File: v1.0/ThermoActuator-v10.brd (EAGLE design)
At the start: 101.6 x 53.3 mm, 18 parts

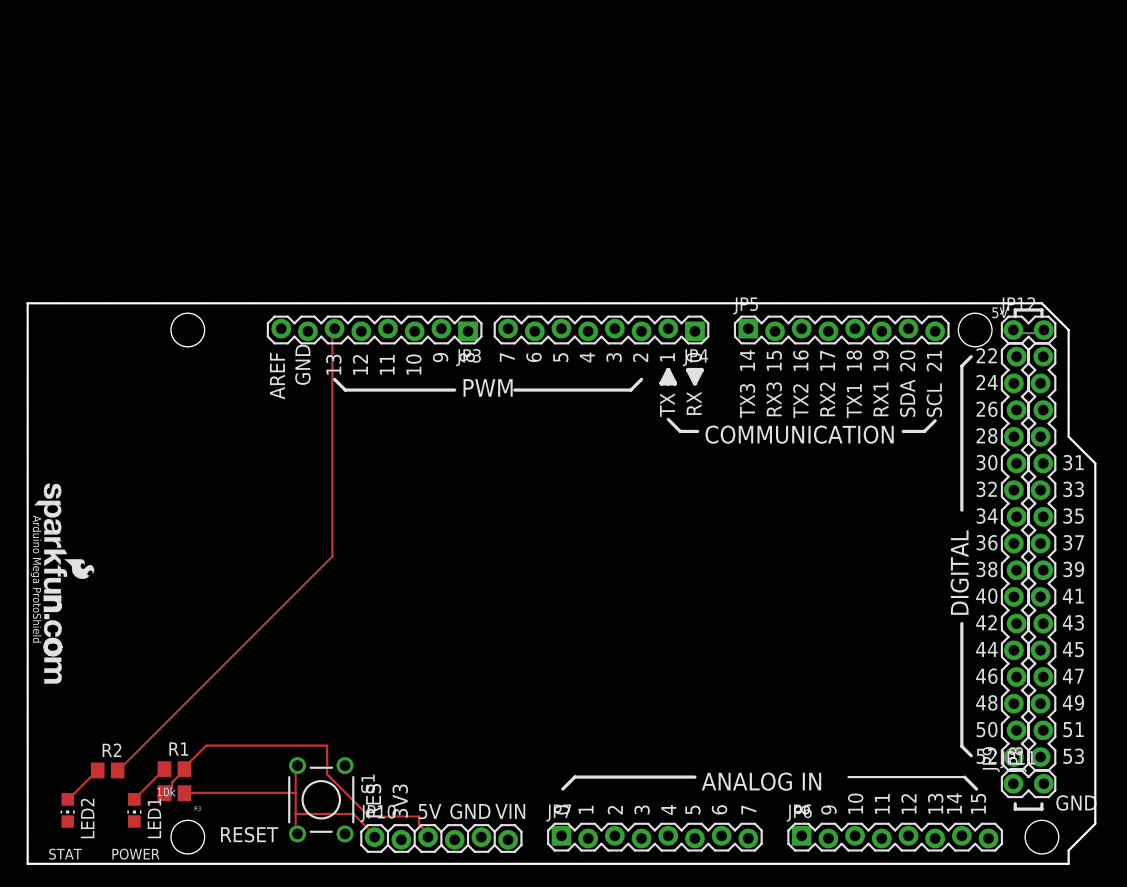
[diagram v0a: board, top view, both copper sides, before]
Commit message: one thermistor ch laid out
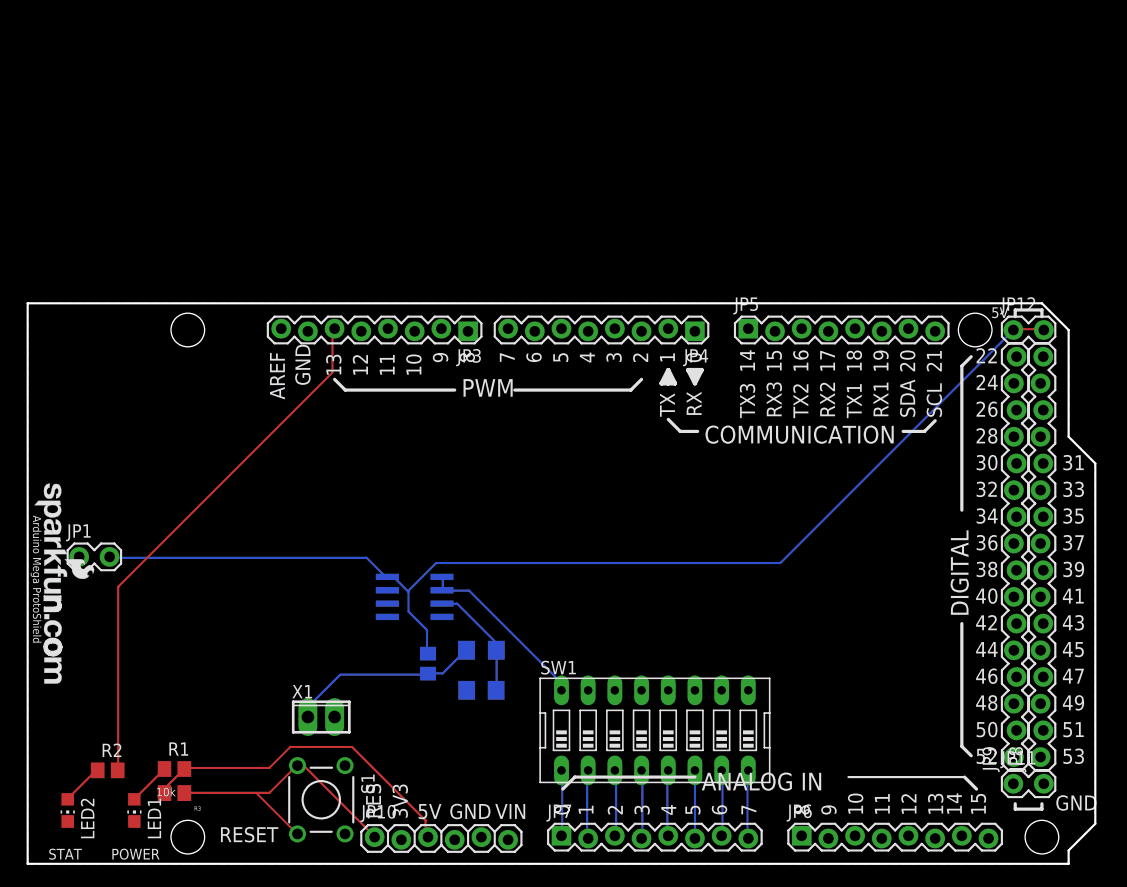
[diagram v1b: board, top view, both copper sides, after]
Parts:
- removed U$2: CREATIVE_COMMONS, SparkFun:CREATIVE_COMMONS
- added C1: 10nF, rcl:C1206
- added IC1: LM358D, linear:SO08
- added JP1: (no value), SparkFun:1X02_LOCK
- added R4: 100K, rcl:R0805
- added R5: 10K, rcl:R1206
- added SW1: (no value), special:EDG-08
- added X1: (no value), con-phoenix-254:2POL254
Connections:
- removed net 5V@1: JP12.1, JP12.2
- removed net A0: JP7.1
- removed net A1: JP7.2
- removed net A2: JP7.3
- removed net A3: JP7.4
- removed net A4: JP7.5
- removed net A5: JP7.6
- removed net A6: JP7.7
- removed net A7: JP7.8
- new net AS0: IC1.1, IC1.2, SW1.16
- new net N$1: R4.1, R5.1, X1.1
- new net N$10: JP7.8, SW1.8
- new net N$2: C1.2, IC1.3, R5.2
- new net N$3: JP7.1, SW1.1
- new net N$4: JP7.2, SW1.2
- new net N$5: JP7.3, SW1.3
- new net N$6: JP7.4, SW1.4
- new net N$7: JP7.5, SW1.5
- new net N$8: JP7.6, SW1.6
- new net N$9: JP7.7, SW1.7
- new net VDD: IC1.8, JP1.2, JP12.1, JP12.2, R4.2
- net GND: now also C1.1, IC1.4, X1.2
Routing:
- net VDD: track 0.00 -> 107.5 mm
- net N$1: track 0.00 -> 18.4 mm
- net AS0: track 0.00 -> 17.0 mm
- net N$2: track 0.00 -> 11.3 mm
- net N$4: track 0.00 -> 6.59 mm
- net N$6: track 0.00 -> 6.57 mm
- net N$10: track 0.00 -> 6.57 mm
- net N$8: track 0.00 -> 6.48 mm
- net N$5: track 0.00 -> 6.39 mm
- net N$7: track 0.00 -> 6.33 mm
- net N$9: track 0.00 -> 6.33 mm
- net N$3: track 0.00 -> 6.31 mm
- net 5V@1: track 3.12 -> 0.00 mm
- net RES: track 25.8 -> 27.6 mm
- net 5V: track 33.3 -> 31.6 mm

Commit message: two channels laid out
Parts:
- added C2: 10nF, rcl:C1206
- added R6: 100K, rcl:R0805
- added R7: 10K, rcl:R1206
- added X2: (no value), con-phoenix-254:2POL254
- moved X1 15.2 mm to (43.2, 14.0)
- moved JP1 14.2 mm to (19.1, 31.8)
- moved C1 8.98 mm to (44.5, 25.4)
- moved R1 2.84 mm to (15.2, 11.6)
- moved R3 2.54 mm to (16.5, 6.73)
- moved R5 1.27 mm to (43.2, 19.1), turned to 90 degrees
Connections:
- new net AS1: IC1.6, IC1.7, SW1.15
- new net N$11: R6.1, R7.1, X2.1
- new net N$12: C2.2, IC1.5, R7.2
- net GND: now also C2.1, X2.2
- net VDD: now also R6.2
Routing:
- net AS1: track 0.00 -> 61.6 mm
- net N$11: track 0.00 -> 12.1 mm
- net N$12: track 0.00 -> 10.6 mm
- net N$1: track 18.4 -> 9.54 mm
- net VDD: track 107.5 -> 99.9 mm
- net AS0: track 17.0 -> 21.0 mm
- net N$126: track 4.07 -> 7.13 mm
- net RES: track 27.6 -> 25.0 mm
- net GND: track 0.00 -> 0.83 mm
- net N$2: track 11.3 -> 12.0 mm

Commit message: shield centered
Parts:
- moved C2 14.0 mm to (27.9, 38.1)
- moved JP10 14.0 mm to (33.0, 16.5)
- moved JP6 14.0 mm to (73.7, 16.5)
- moved JP7 14.0 mm to (50.8, 16.5)
- moved R4 14.0 mm to (38.1, 33.0)
- moved R5 14.0 mm to (43.2, 33.0)
- moved R6 14.0 mm to (33.0, 33.0)
- moved SW1 14.0 mm to (59.7, 26.7)
- moved LED1 14.0 mm to (10.2, 19.1)
- moved LED2 14.0 mm to (3.81, 19.1)
- moved R1 14.0 mm to (15.2, 25.5)
- moved R3 14.0 mm to (16.5, 20.7)
- moved X1 14.0 mm to (43.2, 27.9)
- moved X2 14.0 mm to (38.1, 27.9)
- moved IC1 14.0 mm to (36.8, 39.4)
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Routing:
- net N$13: track 0.00 -> 180.0 mm
- net VDD: track 99.9 -> 0.00 mm
- net AS1: track 61.6 -> 0.00 mm
- net D13: track 50.6 -> 0.00 mm
- net 5V: track 31.7 -> 0.00 mm
- net RES: track 25.0 -> 0.00 mm
- net AS0: track 21.0 -> 0.00 mm
- net N$11: track 12.1 -> 0.00 mm
- net N$2: track 12.0 -> 0.00 mm
- net N$12: track 10.6 -> 0.00 mm
- net N$1: track 9.54 -> 0.00 mm
- net N$126: track 7.13 -> 0.00 mm
- net N$4: track 6.59 -> 0.00 mm
- net N$6: track 6.57 -> 0.00 mm
- net N$10: track 6.57 -> 0.00 mm
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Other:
- board size 101.6 x 53.3 mm -> 100 x 80 mm
- board text removed: "31"
- board text removed: "33"
- board text removed: "35"
- board text removed: "37"
- board text removed: "39"
- board text removed: "41"
- board text removed: "43"
- board text removed: "45"
- board text removed: "47"
- board text removed: "49"
- board text removed: "51"
- board text removed: "53"

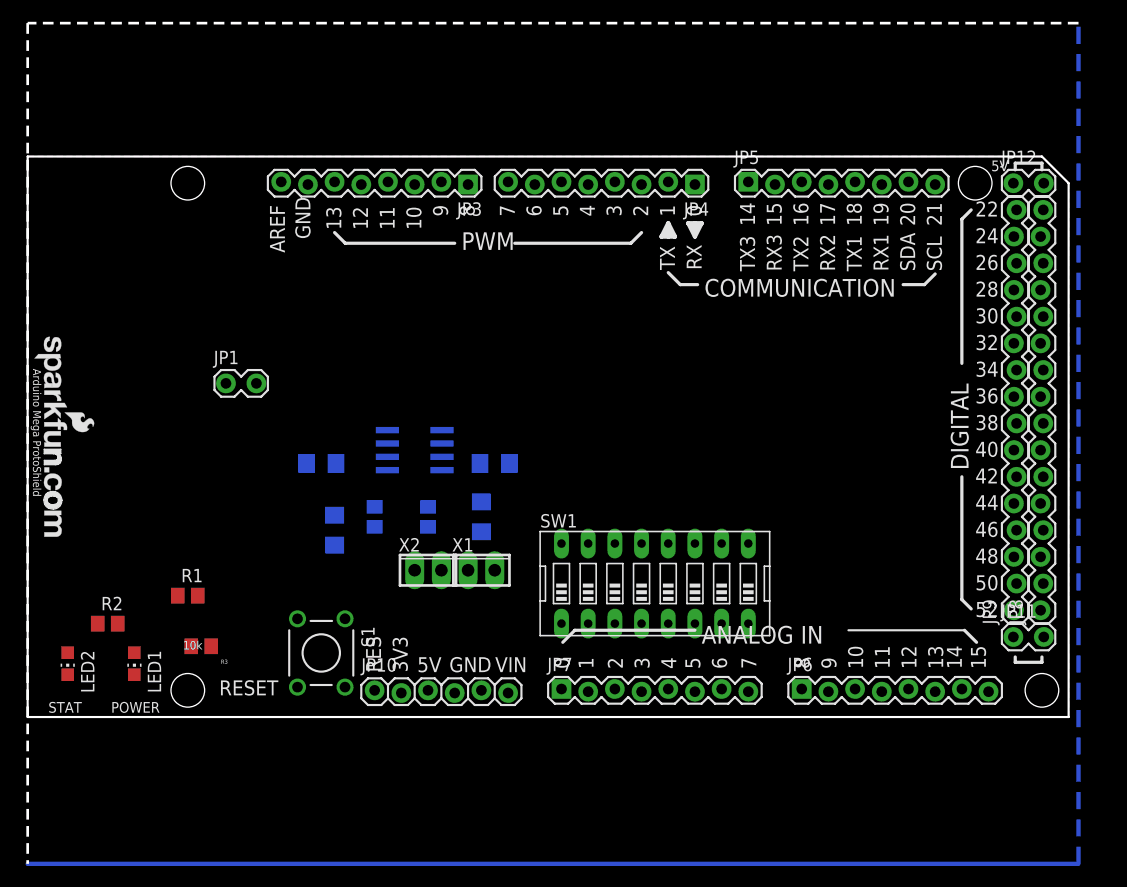
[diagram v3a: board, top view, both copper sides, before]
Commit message: centered with the right edge untouched
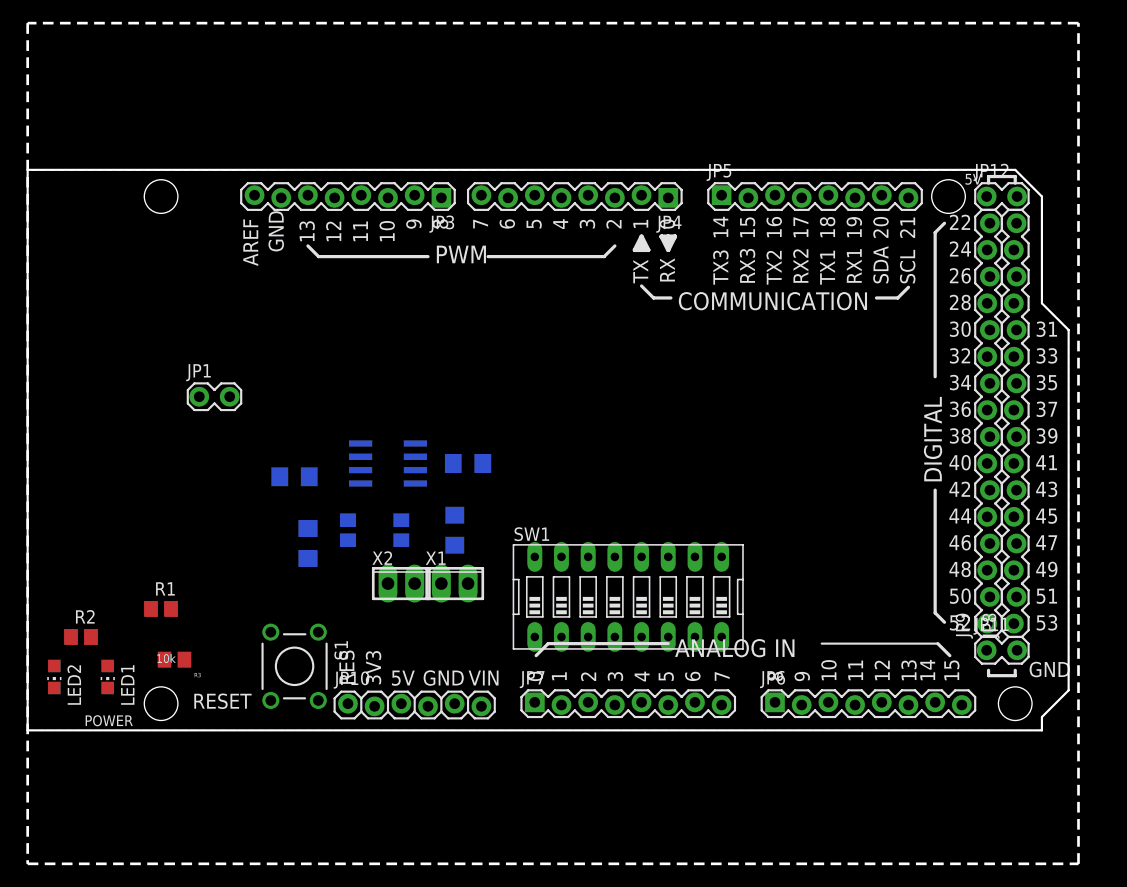
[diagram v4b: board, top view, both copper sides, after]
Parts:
- removed U$1: LOGO-SFENEW, SparkFun:SFE-NEW-WEBLOGO
- moved JP11 2.84 mm to (91.4, 20.3)
- moved JP9 2.84 mm to (91.4, 22.9)
- moved C2 2.84 mm to (25.4, 36.8)
- moved JP12 2.84 mm to (91.4, 63.5)
- moved R6 2.84 mm to (30.5, 31.8)
- moved JP10 2.84 mm to (30.5, 15.2)
- moved S1 2.84 mm to (25.4, 18.8)
- moved R1 2.84 mm to (12.7, 24.3)
- moved R3 2.84 mm to (14.0, 19.4)
- moved R4 2.84 mm to (35.6, 31.8)
- moved R5 2.84 mm to (40.6, 31.8)
- moved SW1 2.84 mm to (57.1, 25.4)
- moved JP7 2.84 mm to (48.3, 15.2)
- moved LED1 2.84 mm to (7.62, 17.8)
- moved R2 2.84 mm to (5.08, 21.6)
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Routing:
- net N$13: track 180.0 -> 0.00 mm
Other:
- outline, holes or cut-outs redrawn
- board text added: "31"
- board text added: "33"
- board text added: "35"
- board text added: "37"
- board text added: "39"
- board text added: "41"
- board text added: "43"
- board text added: "45"
- board text added: "47"
- board text added: "49"
- board text added: "51"
- board text added: "53"
- board text removed: "Arduino Mega ProtoShield"
- board text removed: "STAT"

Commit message: lower edge extended
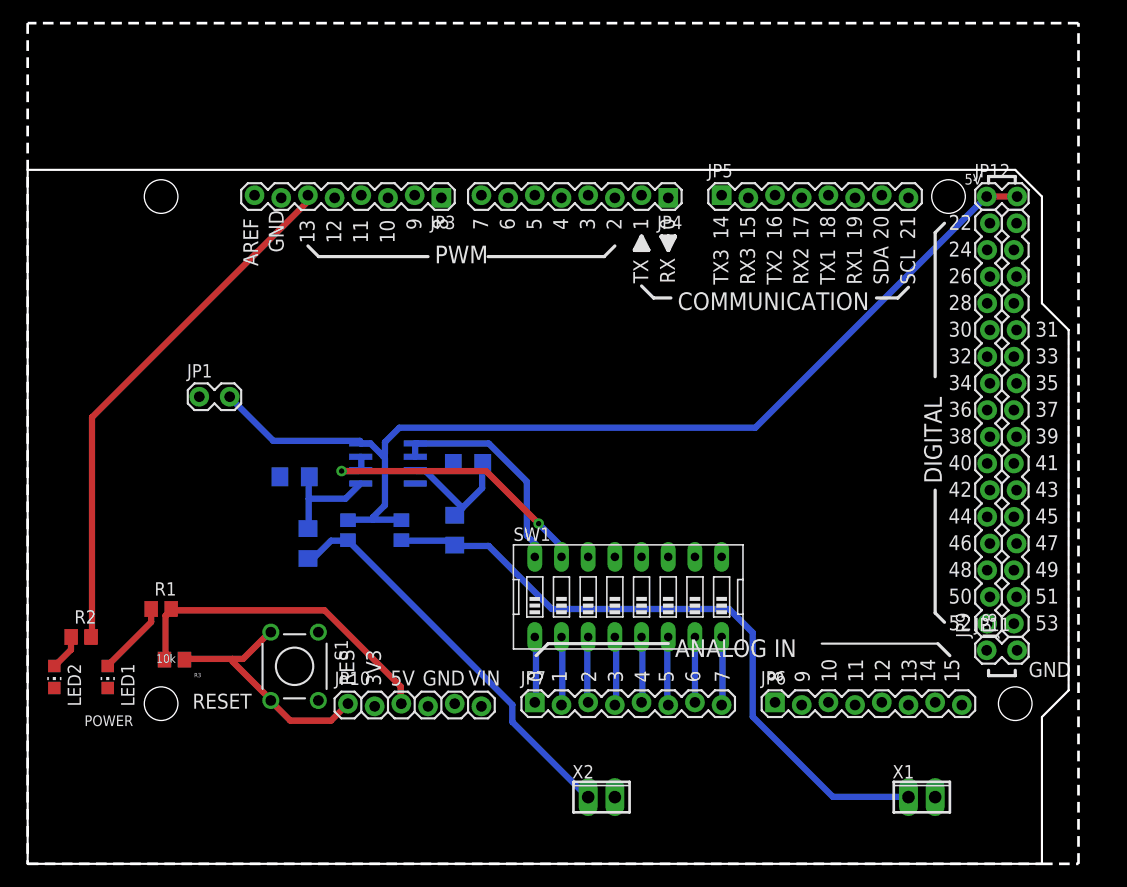
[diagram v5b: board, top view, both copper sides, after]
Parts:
- moved X1 48.9 mm to (85.1, 6.35)
- moved X2 27.9 mm to (54.6, 6.35)
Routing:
- net VDD: track 0.00 -> 100.0 mm
- net N$1: track 0.00 -> 63.1 mm
- net D13: track 0.00 -> 50.6 mm
- net N$11: track 0.00 -> 38.5 mm
- net 5V: track 0.00 -> 31.8 mm
- net AS1: track 0.00 -> 28.0 mm, vias 0 -> 2
- net RES: track 0.00 -> 23.7 mm
- net AS0: track 0.00 -> 21.0 mm
- net N$2: track 0.00 -> 12.0 mm
- net N$12: track 0.00 -> 10.5 mm
- net N$126: track 0.00 -> 7.14 mm
- net N$6: track 0.00 -> 6.65 mm
- net N$8: track 0.00 -> 6.58 mm
- net N$10: track 0.00 -> 6.58 mm
- net N$4: track 0.00 -> 6.57 mm
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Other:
- outline, holes or cut-outs redrawn

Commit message: 4 ADC channels and 8 actuators
somewhat messy, 20 vias. The sparkfun's recommended drc used
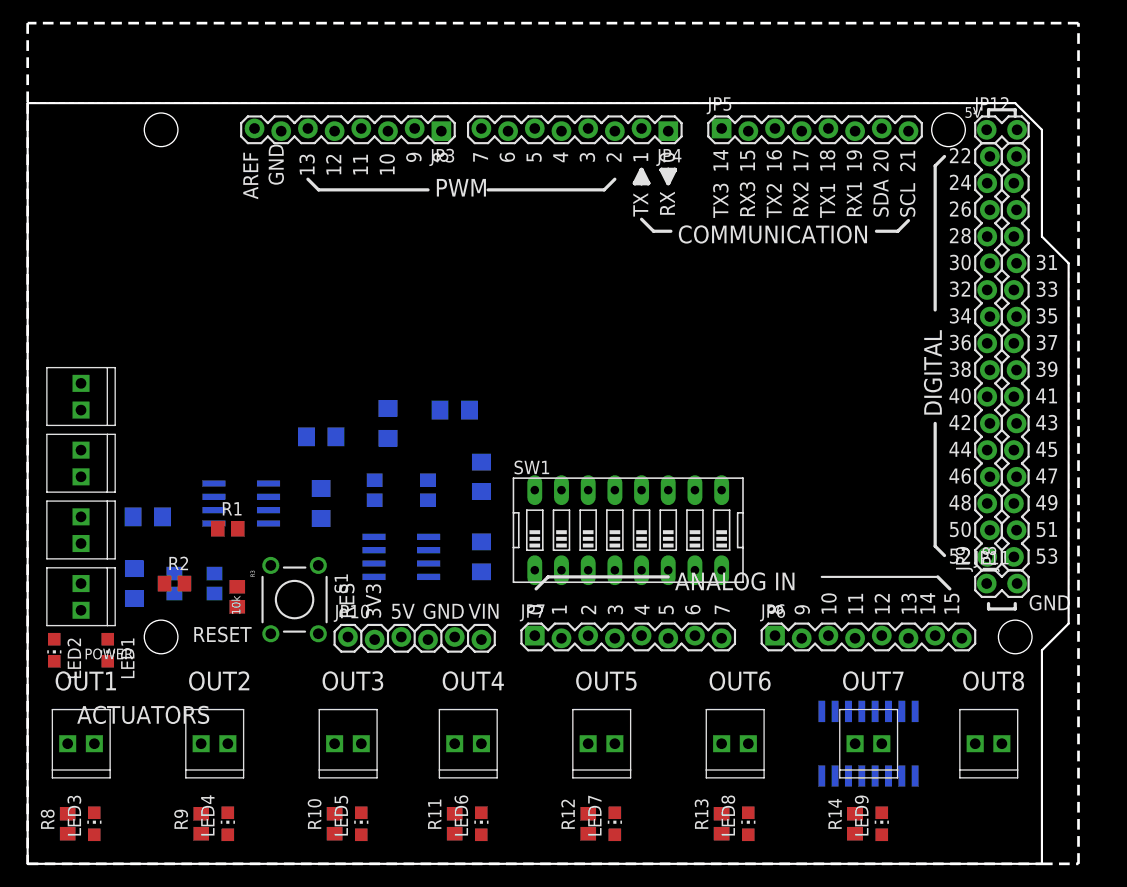
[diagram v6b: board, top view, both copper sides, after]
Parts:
- removed JP1: (no value), SparkFun:1X02_LOCK
- removed X1, X2: (no value), con-phoenix-254:2POL254
- added C3, C4: 10nF, rcl:C1206
- added IC2: ULN2003AD, uln-udn:SO16
- added IC3: LM358D, linear:SO08
- added JP13, JP16, JP17, JP18, JP19, JP20, JP21, JP22, JP23: ADC2, SparkFun-Connectors:1X02_2.54_SCREWTERM
- added JP14: OUT1, SparkFun-Connectors:1X02_2.54_SCREWTERM
- added JP15: OUT2, SparkFun-Connectors:1X02_2.54_SCREWTERM
- added JP2: ADC1, SparkFun-Connectors:1X02_2.54_SCREWTERM
- added LED3, LED4, LED5, LED6, LED7, LED8, LED9: Blue, led:CHIP-LED0805
- added R10, R11, R12, R13, R14, R8, R9: 330, rcl:R0805
- added R15, R17: 100K, rcl:R0805
- added R16, R18: 10K, rcl:R1206
- moved R4 18.5 mm to (17.8, 26.7)
- moved R6 17.3 mm to (14.0, 26.7), turned to 270 degrees
- moved R7 16.9 mm to (10.2, 26.7)
- moved IC1 14.5 mm to (20.3, 34.3), turned to 90 degrees
- moved C2 14.5 mm to (11.4, 33.0), turned to 0 degrees
- moved C1 14.2 mm to (27.9, 40.6)
- moved R5 13.0 mm to (27.9, 34.3)
- moved R2 10.2 mm to (14.0, 26.7)
- moved R1 9.92 mm to (19.1, 31.9)
- moved R3 8.44 mm to (19.9, 25.4), turned to 270 degrees
- moved JP11 6.35 mm to (91.4, 26.7)
- moved JP8 6.35 mm to (94.0, 29.2)
- moved JP9 6.35 mm to (91.4, 29.2)
- moved S1 6.35 mm to (25.4, 25.1)
- moved SW1 6.35 mm to (57.1, 31.8)
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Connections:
- removed net A15: JP6.8
- new net AO0: IC2.16, JP14.P2, LED3.C
- new net AO1: IC2.15, JP15.P2, LED4.C
- new net AO2: IC2.14, JP16.P2, LED5.C
- new net AO3: IC2.13, JP17.P2, LED6.C
- new net AO4: IC2.12, JP18.P2, LED7.C
- new net AO5: IC2.11, JP19.P2, LED8.C
- new net AO6: IC2.10, JP20.P2, LED9.C
- new net AO7: JP21.P2, JP6.8
- new net AS2: IC3.1, IC3.2, SW1.14
- new net AS3: IC3.6, IC3.7, SW1.13
- new net N$13: LED3.A, R8.1
- new net N$14: LED4.A, R9.1
- new net N$15: LED5.A, R10.1
- new net N$16: LED6.A, R11.1
- new net N$17: LED7.A, R12.1
- new net N$18: LED8.A, R13.1
- new net N$19: LED9.A, R14.1
- new net N$20: JP22.P2, R15.1, R16.1
- new net N$21: C3.2, IC3.3, R16.2
- new net N$22: JP23.P2, R17.1, R18.1
- new net N$23: C4.2, IC3.5, R18.2
- net A10: now also IC2.3
- net A11: now also IC2.4
- net A12: now also IC2.5
- net A13: now also IC2.6
- net A14: now also IC2.7
- net A8: now also IC2.1
- net A9: now also IC2.2
- net GND: now also C3.1, C4.1, IC2.8, IC3.4, JP13.P1, JP2.P1, JP21.P1, JP22.P1, JP23.P1; no longer X1.2, X2.2
- net N$1: now also JP2.P2; no longer X1.1
- net N$11: now also JP13.P2; no longer X2.1
- net VDD: now also IC2.9, IC3.8, JP14.P1, JP15.P1, JP16.P1, JP17.P1, JP18.P1, JP19.P1, JP20.P1, R10.2, R11.2, R12.2, R13.2, R14.2, R15.2, R17.2, R8.2, R9.2; no longer JP1.2
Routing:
- net VDD: track 100.0 -> 0.00 mm
- net N$1: track 63.1 -> 0.00 mm
- net D13: track 50.6 -> 0.00 mm
- net N$11: track 38.5 -> 0.00 mm
- net 5V: track 31.8 -> 0.00 mm
- net AS1: track 28.0 -> 0.00 mm, vias 2 -> 0
- net RES: track 23.7 -> 0.00 mm
- net AS0: track 21.0 -> 0.00 mm
- net N$2: track 12.0 -> 0.00 mm
- net N$12: track 10.5 -> 0.00 mm
- net N$126: track 7.14 -> 0.00 mm
- net N$6: track 6.65 -> 0.00 mm
- net N$8: track 6.58 -> 0.00 mm
- net N$10: track 6.58 -> 0.00 mm
- net N$4: track 6.57 -> 0.00 mm
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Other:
- outline, holes or cut-outs redrawn
- board text added: "ACTUATORS"
- board text added: "OUT1"
- board text added: "OUT2"
- board text added: "OUT3"
- board text added: "OUT4"
- board text added: "OUT5"
- board text added: "OUT6"
- board text added: "OUT7"
- board text added: "OUT8"

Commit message: down to 126 DRC errors
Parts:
- R3: value 10k -> (none)
- moved LED2 14.0 mm to (16.5, 21.6)
- moved LED1 12.8 mm to (20.3, 21.6)
- moved C2 6.48 mm to (12.7, 39.4), turned to 270 degrees
- moved R7 5.68 mm to (12.7, 31.8)
- moved JP13 2.84 mm to (6.35, 24.1)
- moved JP22 2.84 mm to (6.35, 30.5)
- moved JP2 2.84 mm to (6.35, 43.2)
- moved JP23 2.84 mm to (6.35, 36.8)
- moved R6 2.54 mm to (16.5, 26.7)
- moved R4 2.54 mm to (20.3, 26.7)
- moved R3 1.80 mm to (18.7, 26.7)
- moved R13 1.27 mm to (64.8, 3.81)
- moved R11 1.27 mm to (39.4, 3.81)
- moved R12 1.27 mm to (52.1, 3.81)
- moved R9 1.27 mm to (15.2, 3.81)
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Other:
- board text added: "ADC1"
- board text added: "ADC2"
- board text added: "ADC3"
- board text added: "ADC4"
